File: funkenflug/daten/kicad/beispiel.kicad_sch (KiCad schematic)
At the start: 11 parts, among them Q1 Q_NPN, Q2 Q_NPN, Q3 Q_NPN, Q4 Q_NPN, Q5 Q_NPN, Q6 Q_NPN, Q7 Q_NPN, Q8 Q_NPN, U1 74HC00

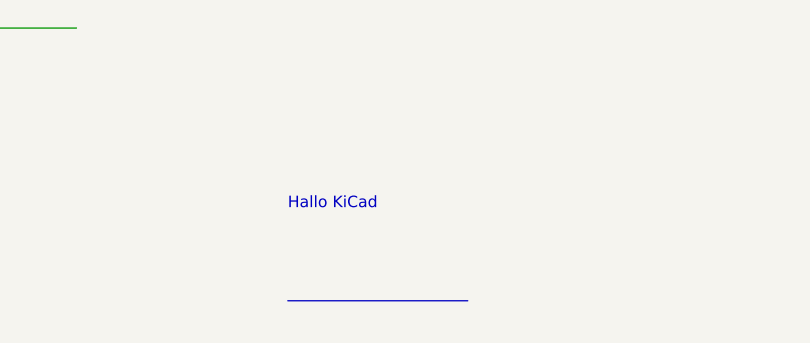
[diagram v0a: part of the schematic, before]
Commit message: funkenflug: Busse im Schaltplan
- kern/busse.dh: Busnamen (D[0..7], A[15:0], Listen, I2C{SDA SCL}),
  Bus-Gruppen, Abzweige, ERC (Abzweig ohne/mit fremdem Label, Pin auf dem
  Bus, Bus ohne/mit unlesbarem/doppeltem Namen), Bus-Ports ueber die
  Blattgrenze je Mitglied; Bus in eigener Liste je Blatt, nie in der
  Netz-Erkennung; Datei (JSON "busse")
- KiCad-Import: Busse mit Name aus dem Label, Bus-Eintraege als Abzweige
- ansicht/busse.dh: Werkzeug Bus (B), Name abfragen, Abzweig fragt nach dem
  naechsten freien Mitglied und setzt das Label; Auswahl, Ziehen und Drehen
  mit folgenden Abzweigen, Loeschen, Ablage
- pruef_kern + Selbsttest (312 Pruefungen)

Co-Authored-By: Claude Opus 5.5 <noreply@anthropic.com>
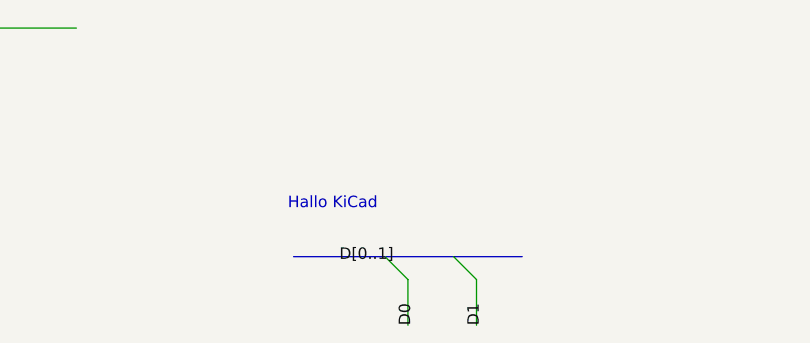
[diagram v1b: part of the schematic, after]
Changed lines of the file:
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@@
     (pin "EIN" input (at 152.4 93.98 180) (effects (font (size 1.27 1.27)) (justify left)))
     (pin "AUS" output (at 177.8 93.98 0) (effects (font (size 1.27 1.27)) (justify right)))
-    (instances (project "beispiel" (path "/0eda425e-f5d9-4d6f-a503-4825a401da80" (page "2"))))
+    (instances (project "beispiel" (path "/54559382-1cf6-4eb9-b0a1-72291336c150" (page "2"))))
   )
   (wire (pts (xy 142.24 93.98) (xy 152.4 93.98)) (stroke (width 0) (type default)))
@@
   (label "SIG_AUS" (at 187.96 93.98 0) (effects (font (size 1.27 1.27)) (justify left)))
   (text "Hallo KiCad" (at 120 160 0) (effects (font (size 1.27 1.27)) (justify left bottom)))
-  (bus (pts (xy 120 170) (xy 140 170)) (stroke (width 0) (type default)))
+  (bus (pts (xy 120.65 165.1) (xy 146.05 165.1)) (stroke (width 0) (type default)))
+  (label "D[0..1]" (at 125.73 165.1 0) (effects (font (size 1.27 1.27)) (justify left)))
+  (bus_entry (at 130.81 165.1) (size 2.54 2.54) (stroke (width 0) (type default)))
+  (wire (pts (xy 133.35 167.64) (xy 133.35 172.72)) (stroke (width 0) (type default)))
+  (label "D0" (at 133.35 172.72 270) (effects (font (size 1.27 1.27)) (justify left)))
+  (bus_entry (at 138.43 165.1) (size 2.54 2.54) (stroke (width 0) (type default)))
+  (wire (pts (xy 140.97 167.64) (xy 140.97 172.72)) (stroke (width 0) (type default)))
+  (label "D1" (at 140.97 172.72 270) (effects (font (size 1.27 1.27)) (justify left)))
+  (bus_alias "ADR" (members "A0" "A1"))
   (symbol (lib_id "Test:Q_NPN") (at 25.4 50.8 0) (unit 1) (in_bom yes) (on_board yes) (dnp no)
     (property "Reference" "Q1" (at 29.21 48.26 0) (effects (font (size 1.27 1.27))))
     (property "Value" "Q_NPN" (at 29.21 53.34 0) (effects (font (size 1.27 1.27))))
     (property "Footprint" "Package_TO_SOT_THT:TO-92_Inline" (at 0 0 0) (effects (font (size 1.27 1.27)) hide))
-    (instances (project "beispiel" (path "/0eda425e-f5d9-4d6f-a503-4825a401da80" (reference "Q1") (unit 1))))
+    (instances (project "beispiel" (path "/54559382-1cf6-4eb9-b0a1-72291336c150" (reference "Q1") (unit 1))))
   )
   (symbol (lib_id "Test:Q_NPN") (at 50.8 50.8 90) (unit 1) (in_bom yes) (on_board yes) (dnp no)
@@
     (property "Value" "Q_NPN" (at 54.61 53.34 0) (effects (font (size 1.27 1.27))))
     (property "Footprint" "Package_TO_SOT_THT:TO-92_Inline" (at 0 0 0) (effects (font (size 1.27 1.27)) hide))
-    (instances (project "beispiel" (path "/0eda425e-f5d9-4d6f-a503-4825a401da80" (reference "Q2") (unit 1))))
+    (instances (project "beispiel" (path "/54559382-1cf6-4eb9-b0a1-72291336c150" (reference "Q2") (unit 1))))
   )
   (symbol (lib_id "Test:Q_NPN") (at 76.2 50.8 180) (unit 1) (in_bom yes) (on_board yes) (dnp no)
@@
     (property "Value" "Q_NPN" (at 80.01 53.34 0) (effects (font (size 1.27 1.27))))
     (property "Footprint" "Package_TO_SOT_THT:TO-92_Inline" (at 0 0 0) (effects (font (size 1.27 1.27)) hide))
-    (instances (project "beispiel" (path "/0eda425e-f5d9-4d6f-a503-4825a401da80" (reference "Q3") (unit 1))))
+    (instances (project "beispiel" (path "/54559382-1cf6-4eb9-b0a1-72291336c150" (reference "Q3") (unit 1))))
   )
   (symbol (lib_id "Test:Q_NPN") (at 101.6 50.8 270) (unit 1) (in_bom yes) (on_board yes) (dnp no)
@@
     (property "Value" "Q_NPN" (at 105.41 53.34 0) (effects (font (size 1.27 1.27))))
     (property "Footprint" "Package_TO_SOT_THT:TO-92_Inline" (at 0 0 0) (effects (font (size 1.27 1.27)) hide))
-    (instances (project "beispiel" (path "/0eda425e-f5d9-4d6f-a503-4825a401da80" (reference "Q4") (unit 1))))
+    (instances (project "beispiel" (path "/54559382-1cf6-4eb9-b0a1-72291336c150" (reference "Q4") (unit 1))))
   )
   (symbol (lib_id "Test:Q_NPN") (at 127 50.8 0) (mirror y) (unit 1) (in_bom yes) (on_board yes) (dnp no)
@@
     (property "Value" "Q_NPN" (at 130.81 53.34 0) (effects (font (size 1.27 1.27))))
     (property "Footprint" "Package_TO_SOT_THT:TO-92_Inline" (at 0 0 0) (effects (font (size 1.27 1.27)) hide))
-    (instances (project "beispiel" (path "/0eda425e-f5d9-4d6f-a503-4825a401da80" (reference "Q5") (unit 1))))
+    (instances (project "beispiel" (path "/54559382-1cf6-4eb9-b0a1-72291336c150" (reference "Q5") (unit 1))))
   )
   (symbol (lib_id "Test:Q_NPN") (at 152.4 50.8 90) (mirror x) (unit 1) (in_bom yes) (on_board yes) (dnp no)
@@
     (property "Value" "Q_NPN" (at 156.21 53.34 0) (effects (font (size 1.27 1.27))))
     (property "Footprint" "Package_TO_SOT_THT:TO-92_Inline" (at 0 0 0) (effects (font (size 1.27 1.27)) hide))
-    (instances (project "beispiel" (path "/0eda425e-f5d9-4d6f-a503-4825a401da80" (reference "Q6") (unit 1))))
+    (instances (project "beispiel" (path "/54559382-1cf6-4eb9-b0a1-72291336c150" (reference "Q6") (unit 1))))
   )
   (symbol (lib_id "Test:Q_NPN") (at 177.8 50.8 180) (mirror y) (unit 1) (in_bom yes) (on_board yes) (dnp no)
@@
     (property "Value" "Q_NPN" (at 181.61 53.34 0) (effects (font (size 1.27 1.27))))
     (property "Footprint" "Package_TO_SOT_THT:TO-92_Inline" (at 0 0 0) (effects (font (size 1.27 1.27)) hide))
-    (instances (project "beispiel" (path "/0eda425e-f5d9-4d6f-a503-4825a401da80" (reference "Q7") (unit 1))))
+    (instances (project "beispiel" (path "/54559382-1cf6-4eb9-b0a1-72291336c150" (reference "Q7") (unit 1))))
   )
   (symbol (lib_id "Test:Q_NPN") (at 203.2 50.8 270) (mirror x) (unit 1) (in_bom yes) (on_board yes) (dnp no)
@@
     (property "Value" "Q_NPN" (at 207.01 53.34 0) (effects (font (size 1.27 1.27))))
     (property "Footprint" "Package_TO_SOT_THT:TO-92_Inline" (at 0 0 0) (effects (font (size 1.27 1.27)) hide))
-    (instances (project "beispiel" (path "/0eda425e-f5d9-4d6f-a503-4825a401da80" (reference "Q8") (unit 1))))
+    (instances (project "beispiel" (path "/54559382-1cf6-4eb9-b0a1-72291336c150" (reference "Q8") (unit 1))))
   )
   (symbol (lib_id "Device:R") (at 25.4 88.9 0) (unit 1) (in_bom yes) (on_board yes) (dnp no)
@@
     (property "Value" "10k" (at 29.21 91.44 0) (effects (font (size 1.27 1.27))))
     (property "Footprint" "" (at 0 0 0) (effects (font (size 1.27 1.27)) hide))
-    (instances (project "beispiel" (path "/0eda425e-f5d9-4d6f-a503-4825a401da80" (reference "R1") (unit 1))))
+    (instances (project "beispiel" (path "/54559382-1cf6-4eb9-b0a1-72291336c150" (reference "R1") (unit 1))))
   )
   (symbol (lib_id "power:VCC") (at 25.4 78.74 0) (unit 1) (in_bom yes) (on_board yes) (dnp no)
@@
     (property "Value" "VCC" (at 29.21 81.28 0) (effects (font (size 1.27 1.27))))
     (property "Footprint" "" (at 0 0 0) (effects (font (size 1.27 1.27)) hide))
-    (instances (project "beispiel" (path "/0eda425e-f5d9-4d6f-a503-4825a401da80" (reference "#PWR01") (unit 1))))
+    (instances (project "beispiel" (path "/54559382-1cf6-4eb9-b0a1-72291336c150" (reference "#PWR01") (unit 1))))
   )
   (symbol (lib_id "power:GND") (at 25.4 99.06 0) (unit 1) (in_bom yes) (on_board yes) (dnp no)
@@
     (property "Value" "GND" (at 29.21 101.6 0) (effects (font (size 1.27 1.27))))
     (property "Footprint" "" (at 0 0 0) (effects (font (size 1.27 1.27)) hide))
-    (instances (project "beispiel" (path "/0eda425e-f5d9-4d6f-a503-4825a401da80" (reference "#PWR02") (unit 1))))
+    (instances (project "beispiel" (path "/54559382-1cf6-4eb9-b0a1-72291336c150" (reference "#PWR02") (unit 1))))
   )
   (symbol (lib_id "Device:R") (at 50.8 88.9 90) (unit 1) (in_bom yes) (on_board yes) (dnp no)
@@
     (property "Value" "4k7" (at 54.61 91.44 0) (effects (font (size 1.27 1.27))))
     (property "Footprint" "" (at 0 0 0) (effects (font (size 1.27 1.27)) hide))
-    (instances (project "beispiel" (path "/0eda425e-f5d9-4d6f-a503-4825a401da80" (reference "R2") (unit 1))))
+    (instances (project "beispiel" (path "/54559382-1cf6-4eb9-b0a1-72291336c150" (reference "R2") (unit 1))))
   )
   (symbol (lib_id "Test:NAND2") (at 76.2 88.9 0) (unit 1) (in_bom yes) (on_board yes) (dnp no)
@@
     (property "Value" "74HC00" (at 80.01 91.44 0) (effects (font (size 1.27 1.27))))
     (property "Footprint" "Package_DIP:DIP-14_W7.62mm" (at 0 0 0) (effects (font (size 1.27 1.27)) hide))
-    (instances (project "beispiel" (path "/0eda425e-f5d9-4d6f-a503-4825a401da80" (reference "U1") (unit 1))))
+    (instances (project "beispiel" (path "/54559382-1cf6-4eb9-b0a1-72291336c150" (reference "U1") (unit 1))))
   )
   (symbol (lib_id "Test:NAND2") (at 114.3 88.9 0) (unit 2) (in_bom yes) (on_board yes) (dnp no)
@@
     (property "Value" "74HC00" (at 118.11 91.44 0) (effects (font (size 1.27 1.27))))
     (property "Footprint" "Package_DIP:DIP-14_W7.62mm" (at 0 0 0) (effects (font (size 1.27 1.27)) hide))
-    (instances (project "beispiel" (path "/0eda425e-f5d9-4d6f-a503-4825a401da80" (reference "U1") (unit 2))))
+    (instances (project "beispiel" (path "/54559382-1cf6-4eb9-b0a1-72291336c150" (reference "U1") (unit 2))))
   )
 )

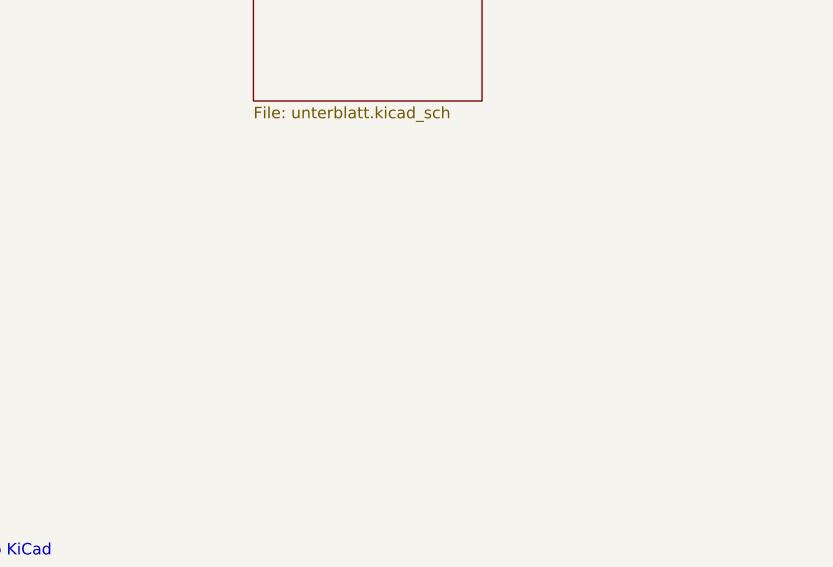
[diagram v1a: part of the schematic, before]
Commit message: funkenflug: Mehrfach-Instanzen von Unterblaettern
- kern/hierarchie.dh: flach() rollt das Dokument aus -- jede weitere Instanz
  eine Kopie mit pfadbasierten Ids und Referenzen (instanzRefs je Pfad,
  sonst R1_2); erste Instanz bleibt das Original; Blattsymbole "Kanal (2)";
  kein Mehrfach-Fehler mehr im ERC
- Netze, ERC (zurueck aufs Original, Instanz am Verstoss, gleiche Meldungen
  einmal), Stueckliste, Netzlisten, Platine, Gerber, 3D und Simulation
  rechnen auf der ausgerollten Sicht; Annotieren schreibt Instanz-Referenzen
- Datei: instanzRefs ("iref"); KiCad-Import: mehrfach eingesetzte Dateien als
  Instanzen, Referenzen aus den KiCad-Instanz-Pfaden (6 und 7)
- ansicht/instanzen.dh: gezeigte Instanz (Doppelklick, Taste I, Elternblatt),
  Referenzen/Netze/ERC-Marker/Statuszeile je Instanz, Referenz je Instanz im
  Eigenschaften-Dialog, Blatt-Menue "Vorhandenes Blatt erneut einsetzen"
- pruef_kern + Selbsttest (322 Pruefungen)

Co-Authored-By: Claude Opus 5.5 <noreply@anthropic.com>
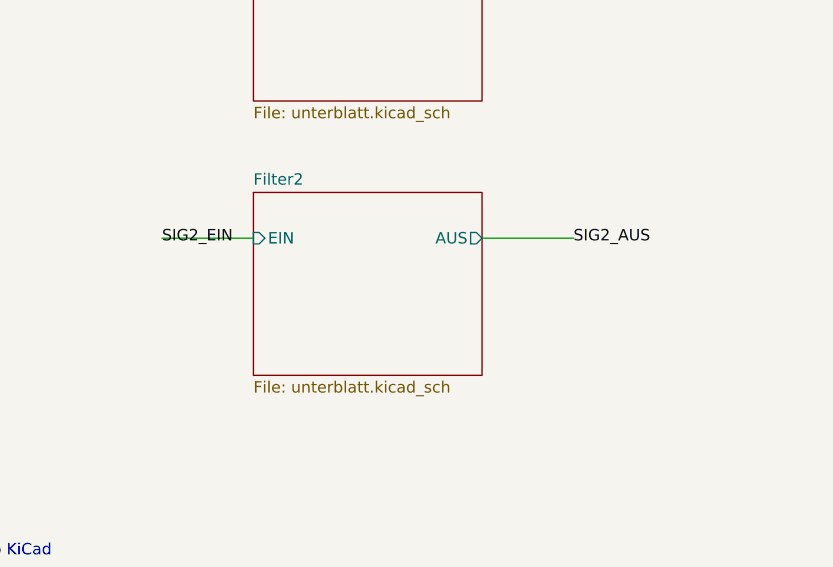
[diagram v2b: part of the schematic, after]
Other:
- added sheet Filter2 (unterblatt.kicad_sch)
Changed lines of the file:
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@@
     (pin "EIN" input (at 152.4 93.98 180) (effects (font (size 1.27 1.27)) (justify left)))
     (pin "AUS" output (at 177.8 93.98 0) (effects (font (size 1.27 1.27)) (justify right)))
-    (instances (project "beispiel" (path "/54559382-1cf6-4eb9-b0a1-72291336c150" (page "2"))))
+    (instances (project "beispiel" (path "/a2ca71bb-2fec-4f2d-b990-42896be89b2e" (page "2"))))
   )
   (wire (pts (xy 142.24 93.98) (xy 152.4 93.98)) (stroke (width 0) (type default)))
@@
   (wire (pts (xy 177.8 93.98) (xy 187.96 93.98)) (stroke (width 0) (type default)))
   (label "SIG_AUS" (at 187.96 93.98 0) (effects (font (size 1.27 1.27)) (justify left)))
+  (sheet (at 152.4 119.38) (size 25.4 20.32) (fields_autoplaced)
+    (stroke (width 0.1524) (type solid)) (fill (color 0 0 0 0.0000))
+    (property "Sheetname" "Filter2" (at 152.4 118.6684 0) (effects (font (size 1.27 1.27)) (justify left bottom)))
+    (property "Sheetfile" "unterblatt.kicad_sch" (at 152.4 140.2846 0) (effects (font (size 1.27 1.27)) (justify left top)))
+    (pin "EIN" input (at 152.4 124.46 180) (effects (font (size 1.27 1.27)) (justify left)))
+    (pin "AUS" output (at 177.8 124.46 0) (effects (font (size 1.27 1.27)) (justify right)))
+    (instances (project "beispiel" (path "/a2ca71bb-2fec-4f2d-b990-42896be89b2e" (page "3"))))
+  )
+  (wire (pts (xy 142.24 124.46) (xy 152.4 124.46)) (stroke (width 0) (type default)))
+  (label "SIG2_EIN" (at 142.24 124.46 180) (effects (font (size 1.27 1.27)) (justify left)))
+  (wire (pts (xy 177.8 124.46) (xy 187.96 124.46)) (stroke (width 0) (type default)))
+  (label "SIG2_AUS" (at 187.96 124.46 0) (effects (font (size 1.27 1.27)) (justify left)))
   (text "Hallo KiCad" (at 120 160 0) (effects (font (size 1.27 1.27)) (justify left bottom)))
   (bus (pts (xy 120.65 165.1) (xy 146.05 165.1)) (stroke (width 0) (type default)))
@@
     (property "Value" "Q_NPN" (at 29.21 53.34 0) (effects (font (size 1.27 1.27))))
     (property "Footprint" "Package_TO_SOT_THT:TO-92_Inline" (at 0 0 0) (effects (font (size 1.27 1.27)) hide))
-    (instances (project "beispiel" (path "/54559382-1cf6-4eb9-b0a1-72291336c150" (reference "Q1") (unit 1))))
+    (instances (project "beispiel" (path "/a2ca71bb-2fec-4f2d-b990-42896be89b2e" (reference "Q1") (unit 1))))
   )
   (symbol (lib_id "Test:Q_NPN") (at 50.8 50.8 90) (unit 1) (in_bom yes) (on_board yes) (dnp no)
@@
     (property "Value" "Q_NPN" (at 54.61 53.34 0) (effects (font (size 1.27 1.27))))
     (property "Footprint" "Package_TO_SOT_THT:TO-92_Inline" (at 0 0 0) (effects (font (size 1.27 1.27)) hide))
-    (instances (project "beispiel" (path "/54559382-1cf6-4eb9-b0a1-72291336c150" (reference "Q2") (unit 1))))
+    (instances (project "beispiel" (path "/a2ca71bb-2fec-4f2d-b990-42896be89b2e" (reference "Q2") (unit 1))))
   )
   (symbol (lib_id "Test:Q_NPN") (at 76.2 50.8 180) (unit 1) (in_bom yes) (on_board yes) (dnp no)
@@
     (property "Value" "Q_NPN" (at 80.01 53.34 0) (effects (font (size 1.27 1.27))))
     (property "Footprint" "Package_TO_SOT_THT:TO-92_Inline" (at 0 0 0) (effects (font (size 1.27 1.27)) hide))
-    (instances (project "beispiel" (path "/54559382-1cf6-4eb9-b0a1-72291336c150" (reference "Q3") (unit 1))))
+    (instances (project "beispiel" (path "/a2ca71bb-2fec-4f2d-b990-42896be89b2e" (reference "Q3") (unit 1))))
   )
   (symbol (lib_id "Test:Q_NPN") (at 101.6 50.8 270) (unit 1) (in_bom yes) (on_board yes) (dnp no)
@@
     (property "Value" "Q_NPN" (at 105.41 53.34 0) (effects (font (size 1.27 1.27))))
     (property "Footprint" "Package_TO_SOT_THT:TO-92_Inline" (at 0 0 0) (effects (font (size 1.27 1.27)) hide))
-    (instances (project "beispiel" (path "/54559382-1cf6-4eb9-b0a1-72291336c150" (reference "Q4") (unit 1))))
+    (instances (project "beispiel" (path "/a2ca71bb-2fec-4f2d-b990-42896be89b2e" (reference "Q4") (unit 1))))
   )
   (symbol (lib_id "Test:Q_NPN") (at 127 50.8 0) (mirror y) (unit 1) (in_bom yes) (on_board yes) (dnp no)
@@
     (property "Value" "Q_NPN" (at 130.81 53.34 0) (effects (font (size 1.27 1.27))))
     (property "Footprint" "Package_TO_SOT_THT:TO-92_Inline" (at 0 0 0) (effects (font (size 1.27 1.27)) hide))
-    (instances (project "beispiel" (path "/54559382-1cf6-4eb9-b0a1-72291336c150" (reference "Q5") (unit 1))))
+    (instances (project "beispiel" (path "/a2ca71bb-2fec-4f2d-b990-42896be89b2e" (reference "Q5") (unit 1))))
   )
   (symbol (lib_id "Test:Q_NPN") (at 152.4 50.8 90) (mirror x) (unit 1) (in_bom yes) (on_board yes) (dnp no)
@@
     (property "Value" "Q_NPN" (at 156.21 53.34 0) (effects (font (size 1.27 1.27))))
     (property "Footprint" "Package_TO_SOT_THT:TO-92_Inline" (at 0 0 0) (effects (font (size 1.27 1.27)) hide))
-    (instances (project "beispiel" (path "/54559382-1cf6-4eb9-b0a1-72291336c150" (reference "Q6") (unit 1))))
+    (instances (project "beispiel" (path "/a2ca71bb-2fec-4f2d-b990-42896be89b2e" (reference "Q6") (unit 1))))
   )
   (symbol (lib_id "Test:Q_NPN") (at 177.8 50.8 180) (mirror y) (unit 1) (in_bom yes) (on_board yes) (dnp no)
@@
     (property "Value" "Q_NPN" (at 181.61 53.34 0) (effects (font (size 1.27 1.27))))
     (property "Footprint" "Package_TO_SOT_THT:TO-92_Inline" (at 0 0 0) (effects (font (size 1.27 1.27)) hide))
-    (instances (project "beispiel" (path "/54559382-1cf6-4eb9-b0a1-72291336c150" (reference "Q7") (unit 1))))
+    (instances (project "beispiel" (path "/a2ca71bb-2fec-4f2d-b990-42896be89b2e" (reference "Q7") (unit 1))))
   )
   (symbol (lib_id "Test:Q_NPN") (at 203.2 50.8 270) (mirror x) (unit 1) (in_bom yes) (on_board yes) (dnp no)
@@
     (property "Value" "Q_NPN" (at 207.01 53.34 0) (effects (font (size 1.27 1.27))))
     (property "Footprint" "Package_TO_SOT_THT:TO-92_Inline" (at 0 0 0) (effects (font (size 1.27 1.27)) hide))
-    (instances (project "beispiel" (path "/54559382-1cf6-4eb9-b0a1-72291336c150" (reference "Q8") (unit 1))))
+    (instances (project "beispiel" (path "/a2ca71bb-2fec-4f2d-b990-42896be89b2e" (reference "Q8") (unit 1))))
   )
   (symbol (lib_id "Device:R") (at 25.4 88.9 0) (unit 1) (in_bom yes) (on_board yes) (dnp no)
@@
     (property "Value" "10k" (at 29.21 91.44 0) (effects (font (size 1.27 1.27))))
     (property "Footprint" "" (at 0 0 0) (effects (font (size 1.27 1.27)) hide))
-    (instances (project "beispiel" (path "/54559382-1cf6-4eb9-b0a1-72291336c150" (reference "R1") (unit 1))))
+    (instances (project "beispiel" (path "/a2ca71bb-2fec-4f2d-b990-42896be89b2e" (reference "R1") (unit 1))))
   )
   (symbol (lib_id "power:VCC") (at 25.4 78.74 0) (unit 1) (in_bom yes) (on_board yes) (dnp no)
@@
     (property "Value" "VCC" (at 29.21 81.28 0) (effects (font (size 1.27 1.27))))
     (property "Footprint" "" (at 0 0 0) (effects (font (size 1.27 1.27)) hide))
-    (instances (project "beispiel" (path "/54559382-1cf6-4eb9-b0a1-72291336c150" (reference "#PWR01") (unit 1))))
+    (instances (project "beispiel" (path "/a2ca71bb-2fec-4f2d-b990-42896be89b2e" (reference "#PWR01") (unit 1))))
   )
   (symbol (lib_id "power:GND") (at 25.4 99.06 0) (unit 1) (in_bom yes) (on_board yes) (dnp no)
@@
     (property "Value" "GND" (at 29.21 101.6 0) (effects (font (size 1.27 1.27))))
     (property "Footprint" "" (at 0 0 0) (effects (font (size 1.27 1.27)) hide))
-    (instances (project "beispiel" (path "/54559382-1cf6-4eb9-b0a1-72291336c150" (reference "#PWR02") (unit 1))))
+    (instances (project "beispiel" (path "/a2ca71bb-2fec-4f2d-b990-42896be89b2e" (reference "#PWR02") (unit 1))))
   )
   (symbol (lib_id "Device:R") (at 50.8 88.9 90) (unit 1) (in_bom yes) (on_board yes) (dnp no)
@@
     (property "Value" "4k7" (at 54.61 91.44 0) (effects (font (size 1.27 1.27))))
     (property "Footprint" "" (at 0 0 0) (effects (font (size 1.27 1.27)) hide))
-    (instances (project "beispiel" (path "/54559382-1cf6-4eb9-b0a1-72291336c150" (reference "R2") (unit 1))))
+    (instances (project "beispiel" (path "/a2ca71bb-2fec-4f2d-b990-42896be89b2e" (reference "R2") (unit 1))))
   )
   (symbol (lib_id "Test:NAND2") (at 76.2 88.9 0) (unit 1) (in_bom yes) (on_board yes) (dnp no)
@@
     (property "Value" "74HC00" (at 80.01 91.44 0) (effects (font (size 1.27 1.27))))
     (property "Footprint" "Package_DIP:DIP-14_W7.62mm" (at 0 0 0) (effects (font (size 1.27 1.27)) hide))
-    (instances (project "beispiel" (path "/54559382-1cf6-4eb9-b0a1-72291336c150" (reference "U1") (unit 1))))
+    (instances (project "beispiel" (path "/a2ca71bb-2fec-4f2d-b990-42896be89b2e" (reference "U1") (unit 1))))
   )
   (symbol (lib_id "Test:NAND2") (at 114.3 88.9 0) (unit 2) (in_bom yes) (on_board yes) (dnp no)
@@
     (property "Value" "74HC00" (at 118.11 91.44 0) (effects (font (size 1.27 1.27))))
     (property "Footprint" "Package_DIP:DIP-14_W7.62mm" (at 0 0 0) (effects (font (size 1.27 1.27)) hide))
-    (instances (project "beispiel" (path "/54559382-1cf6-4eb9-b0a1-72291336c150" (reference "U1") (unit 2))))
+    (instances (project "beispiel" (path "/a2ca71bb-2fec-4f2d-b990-42896be89b2e" (reference "U1") (unit 2))))
   )
 )
